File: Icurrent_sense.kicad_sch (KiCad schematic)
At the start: 5 parts, among them U1 MAX40201FAUA

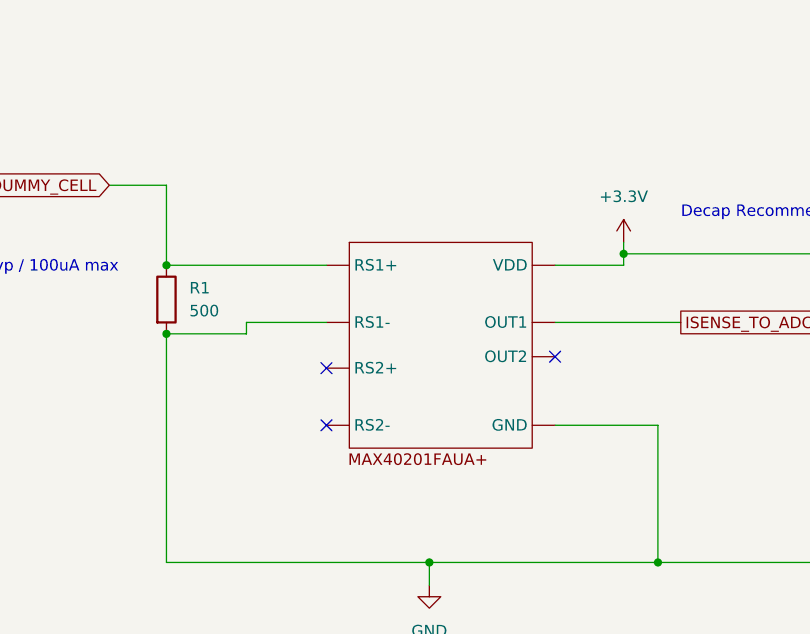
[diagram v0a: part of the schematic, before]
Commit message: ADC swap for multi-channel opamp
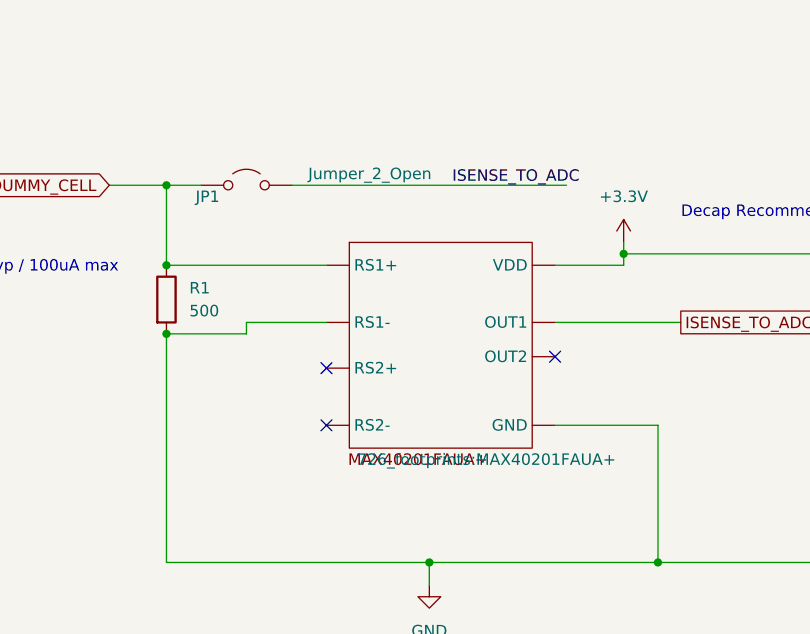
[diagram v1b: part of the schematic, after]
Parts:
- added JP1: Jumper_2_Open, Jumper:SolderJumper-2_P1.3mm_Open_Pad1.0x1.5mm, symbol Jumper:Jumper_2_Open
- U1: footprint (none) -> 726_footprints:MAX40201FAUA+
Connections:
- net IOUT_DUMMY_CELL: now also JP1.1 (A)
- net ISENSE_TO_ADC: now also JP1.2 (B)
